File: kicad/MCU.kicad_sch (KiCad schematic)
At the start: 10 parts, among them U10 STM32G0B1KCUx, U34 SN65HVD230, Y2 CM9V-T1A 32.768 kHz

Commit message: Placed status LEDs
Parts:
- added D42: Status_LED1, symbol Device:LED
- added D43: Status_LED2, symbol Device:LED
- added R76, R77: 150, symbol Device:R
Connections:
- net GND: now also D42.1 (K), D43.1 (K)
- net NRST: now reaches U10.6 (PF2)
- net Status_LED1: no longer names the net of U10.30 (PB6)
- net Status_LED1: now also R76.2
- net Status_LED2: no longer names the net of U10.20 (PC6)
- net Status_LED2: now also R77.2
- new net: D43.2 (A), R77.1
- new net: D42.2 (A), R76.1
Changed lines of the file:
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@@
+    (stroke (width 0) (type default))
+  )
+  (wire (pts (xy 40.64 72.39) (xy 40.64 69.85))
     (stroke (width 0) (type default))
   )
@@
     (stroke (width 0) (type default))
   )
+  (wire (pts (xy 44.45 46.99) (xy 54.61 46.99))
+    (stroke (width 0) (type default))
+  )
   (wire (pts (xy 38.1 74.93) (xy 54.61 74.93))
     (stroke (width 0) (type default))
   )
+  (wire (pts (xy 54.61 72.39) (xy 40.64 72.39))
+    (stroke (width 0) (type default))
+  )
   (wire (pts (xy 151.13 78.74) (xy 151.13 76.2))
     (stroke (width 0) (type default))
   )
+  (wire (pts (xy 40.64 69.85) (xy 39.37 69.85))
+    (stroke (width 0) (type default))
+  )
   (wire (pts (xy 90.17 67.31) (xy 104.14 67.31))
     (stroke (width 0) (type default))
@@
     (stroke (width 0) (type default))
   )
-  (global_label "Status_LED2" (shape output) (at 54.61 46.99 180) (fields_autoplaced)
-    (effects (font (size 1.27 1.27)) (justify right))
-    (property "Intersheetrefs" "${INTERSHEET_REFS}" (at 40.0136 46.99 0)
-      (effects (font (size 1.27 1.27)) (justify right) hide)
-    )
-  )
   (global_label "ChargeEnable" (shape output) (at 54.61 59.69 180) (fields_autoplaced)
     (effects (font (size 1.27 1.27)) (justify right))
@@
     )
   )
+  (global_label "NRST" (shape input) (at 54.61 41.91 180) (fields_autoplaced)
+    (effects (font (size 1.27 1.27)) (justify right))
+    (property "Intersheetrefs" "${INTERSHEET_REFS}" (at 46.8472 41.91 0)
+      (effects (font (size 1.27 1.27)) (justify right) hide)
+    )
+  )
   (global_label "SWDCLK" (shape input) (at 90.17 77.47 0) (fields_autoplaced)
     (effects (font (size 1.27 1.27)) (justify left))
@@
     (effects (font (size 1.27 1.27)) (justify right))
     (property "Intersheetrefs" "${INTERSHEET_REFS}" (at 139.0129 76.2 0)
-      (effects (font (size 1.27 1.27)) (justify right) hide)
-    )
-  )
-  (global_label "Status_LED1" (shape output) (at 54.61 72.39 180) (fields_autoplaced)
-    (effects (font (size 1.27 1.27)) (justify right))
-    (property "Intersheetrefs" "${INTERSHEET_REFS}" (at 40.0136 72.39 0)
       (effects (font (size 1.27 1.27)) (justify right) hide)
     )
@@
         (path "/7f25f26f-13d1-483f-a85d-b3abae309e30/bb4c6abb-96c2-4de6-af9e-637895d0c9f4"
           (reference "C14") (unit 1)
+        )
+      )
+    )
+  )
+  (symbol (lib_id "Device:LED") (at 33.02 46.99 0) (unit 1)
+    (in_bom yes) (on_board yes) (dnp no) (fields_autoplaced)
+    (property "Reference" "D43" (at 31.4325 40.64 0)
+      (effects (font (size 1.27 1.27)))
+    )
+    (property "Value" "Status_LED2" (at 31.4325 43.18 0)
+      (effects (font (size 1.27 1.27)))
+    )
+    (property "Footprint" "" (at 33.02 46.99 0)
+      (effects (font (size 1.27 1.27)) hide)
+    )
+    (property "Datasheet" "~" (at 33.02 46.99 0)
+      (effects (font (size 1.27 1.27)) hide)
+    )
+    (pin "1")
+    (pin "2")
+    (instances
+      (project "sBMS"
+        (path "/7f25f26f-13d1-483f-a85d-b3abae309e30/bb4c6abb-96c2-4de6-af9e-637895d0c9f4"
+          (reference "D43") (unit 1)
         )
       )
@@
     )
   )
+  (symbol (lib_id "Device:R") (at 35.56 69.85 90) (unit 1)
+    (in_bom yes) (on_board yes) (dnp no) (fields_autoplaced)
+    (property "Reference" "R76" (at 35.56 63.5 90)
+      (effects (font (size 1.27 1.27)))
+    )
+    (property "Value" "150" (at 35.56 66.04 90)
+      (effects (font (size 1.27 1.27)))
+    )
+    (property "Footprint" "" (at 35.56 71.628 90)
+      (effects (font (size 1.27 1.27)) hide)
+    )
+    (property "Datasheet" "~" (at 35.56 69.85 0)
+      (effects (font (size 1.27 1.27)) hide)
+    )
+    (pin "1")
+    (pin "2")
+    (instances
+      (project "sBMS"
+        (path "/7f25f26f-13d1-483f-a85d-b3abae309e30/bb4c6abb-96c2-4de6-af9e-637895d0c9f4"
+          (reference "R76") (unit 1)
+        )
+      )
+    )
+  )
   (symbol (lib_id "power:GND") (at 138.43 46.99 270) (unit 1)
     (in_bom yes) (on_board yes) (dnp no) (fields_autoplaced)
@@
     )
   )
+  (symbol (lib_id "Device:LED") (at 27.94 69.85 0) (unit 1)
+    (in_bom yes) (on_board yes) (dnp no) (fields_autoplaced)
+    (property "Reference" "D42" (at 26.3525 63.5 0)
+      (effects (font (size 1.27 1.27)))
+    )
+    (property "Value" "Status_LED1" (at 26.3525 66.04 0)
+      (effects (font (size 1.27 1.27)))
+    )
+    (property "Footprint" "" (at 27.94 69.85 0)
+      (effects (font (size 1.27 1.27)) hide)
+    )
+    (property "Datasheet" "~" (at 27.94 69.85 0)
+      (effects (font (size 1.27 1.27)) hide)
+    )
+    (pin "1")
+    (pin "2")
+    (instances
+      (project "sBMS"
+        (path "/7f25f26f-13d1-483f-a85d-b3abae309e30/bb4c6abb-96c2-4de6-af9e-637895d0c9f4"
+          (reference "D42") (unit 1)
+        )
+      )
+    )
+  )
   (symbol (lib_id "power:+3.3V") (at 111.76 67.31 270) (unit 1)
     (in_bom yes) (on_board yes) (dnp no) (fields_autoplaced)
@@
         )
       )
+    )
+  )
+  (symbol (lib_id "power:GND") (at 29.21 46.99 270) (unit 1)
+    (in_bom yes) (on_board yes) (dnp no) (fields_autoplaced)
+    (property "Reference" "#PWR0154" (at 22.86 46.99 0)
+      (effects (font (size 1.27 1.27)) hide)
+    )
+    (property "Value" "GND" (at 25.4 46.99 90)
+      (effects (font (size 1.27 1.27)) (justify right))
+    )
+    (property "Footprint" "" (at 29.21 46.99 0)
+      (effects (font (size 1.27 1.27)) hide)
+    )
+    (property "Datasheet" "" (at 29.21 46.99 0)
+      (effects (font (size 1.27 1.27)) hide)
+    )
+    (pin "1")
+    (instances
+      (project "sBMS"
+        (path "/7f25f26f-13d1-483f-a85d-b3abae309e30/bb4c6abb-96c2-4de6-af9e-637895d0c9f4"
+          (reference "#PWR0154") (unit 1)
+        )
+      )
+    )
+  )
+  (symbol (lib_id "power:GND") (at 24.13 69.85 270) (unit 1)
+    (in_bom yes) (on_board yes) (dnp no) (fields_autoplaced)
+    (property "Reference" "#PWR0153" (at 17.78 69.85 0)
+      (effects (font (size 1.27 1.27)) hide)
+    )
+    (property "Value" "GND" (at 20.32 69.85 90)
+      (effects (font (size 1.27 1.27)) (justify right))
+    )
+    (property "Footprint" "" (at 24.13 69.85 0)
+      (effects (font (size 1.27 1.27)) hide)
+    )
+    (property "Datasheet" "" (at 24.13 69.85 0)
+      (effects (font (size 1.27 1.27)) hide)
+    )
+    (pin "1")
+    (instances
+      (project "sBMS"
+        (path "/7f25f26f-13d1-483f-a85d-b3abae309e30/bb4c6abb-96c2-4de6-af9e-637895d0c9f4"
+          (reference "#PWR0153") (unit 1)
+        )
+      )
+    )
+  )
+  (symbol (lib_id "Device:R") (at 40.64 46.99 90) (unit 1)
+    (in_bom yes) (on_board yes) (dnp no) (fields_autoplaced)
+    (property "Reference" "R77" (at 40.64 40.64 90)
+      (effects (font (size 1.27 1.27)))
+    )
+    (property "Value" "150" (at 40.64 43.18 90)
+      (effects (font (size 1.27 1.27)))
+    )
+    (property "Footprint" "" (at 40.64 48.768 90)
+      (effects (font (size 1.27 1.27)) hide)
+    )
+    (property "Datasheet" "~" (at 40.64 46.99 0)
+      (effects (font (size 1.27 1.27)) hide)
+    )
+    (pin "1")
+    (pin "2")
+    (instances
+      (project "sBMS"
+        (path "/7f25f26f-13d1-483f-a85d-b3abae309e30/bb4c6abb-96c2-4de6-af9e-637895d0c9f4"
+          (reference "R77") (unit 1)
+        )
+      )

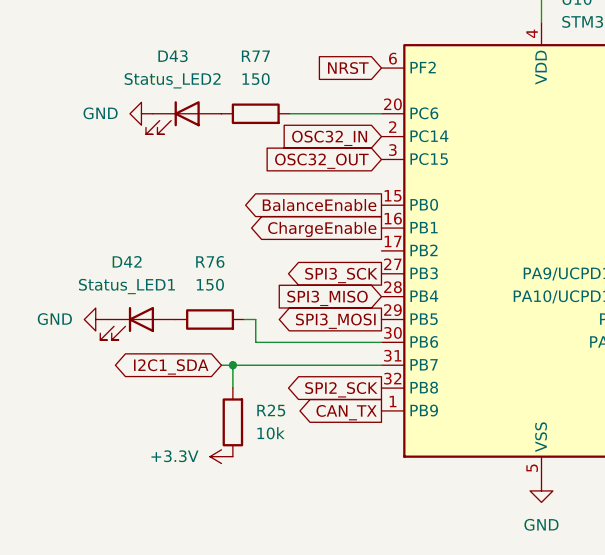
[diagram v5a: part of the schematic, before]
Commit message: Added charge MOSFET
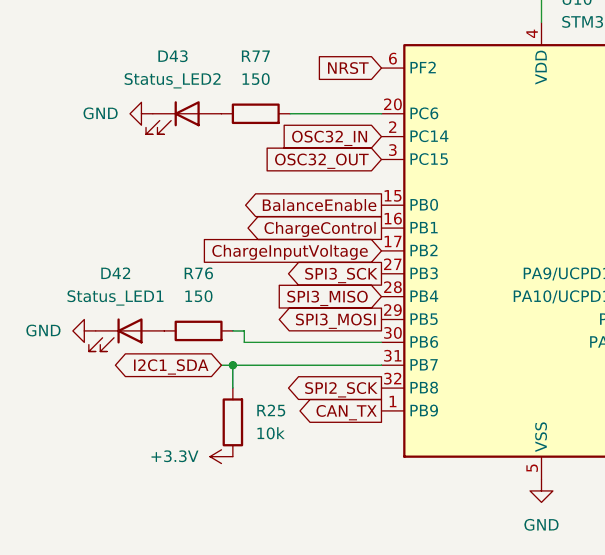
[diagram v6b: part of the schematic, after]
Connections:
- net ChargeInputVoltage: now reaches U10.17 (PB2)
- net ChargeEnable renamed ChargeControl
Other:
- moved on the sheet: D42, R76
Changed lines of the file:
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@@
   (title_block
     (title "Logic")
-    (date "2023-08-20")
+    (date "2023-09-06")
     (rev "1")
     (company "Dynamium")
@@
     (stroke (width 0) (type default))
   )
-  (wire (pts (xy 40.64 72.39) (xy 40.64 69.85))
+  (wire (pts (xy 39.37 72.39) (xy 54.61 72.39))
     (stroke (width 0) (type default))
   )
@@
     (stroke (width 0) (type default))
   )
-  (wire (pts (xy 54.61 72.39) (xy 40.64 72.39))
+  (wire (pts (xy 38.1 71.12) (xy 39.37 71.12))
     (stroke (width 0) (type default))
   )
@@
     (stroke (width 0) (type default))
   )
-  (wire (pts (xy 40.64 69.85) (xy 39.37 69.85))
+  (wire (pts (xy 39.37 71.12) (xy 39.37 72.39))
     (stroke (width 0) (type default))
   )
@@
     (stroke (width 0) (type default))
   )
-  (global_label "ChargeEnable" (shape output) (at 54.61 59.69 180) (fields_autoplaced)
-    (effects (font (size 1.27 1.27)) (justify right))
-    (property "Intersheetrefs" "${INTERSHEET_REFS}" (at 38.6832 59.69 0)
+  (global_label "ChargeControl" (shape output) (at 54.61 59.69 180) (fields_autoplaced)
+    (effects (font (size 1.27 1.27)) (justify right))
+    (property "Intersheetrefs" "${INTERSHEET_REFS}" (at 38.1389 59.69 0)
       (effects (font (size 1.27 1.27)) (justify right) hide)
     )
@@
     (property "Intersheetrefs" "${INTERSHEET_REFS}" (at 175.3424 44.45 0)
       (effects (font (size 1.27 1.27)) (justify left) hide)
+    )
+  )
+  (global_label "ChargeInputVoltage" (shape input) (at 54.61 62.23 180) (fields_autoplaced)
+    (effects (font (size 1.27 1.27)) (justify right))
+    (property "Intersheetrefs" "${INTERSHEET_REFS}" (at 33.2404 62.23 0)
+      (effects (font (size 1.27 1.27)) (justify right) hide)
     )
   )
@@
     )
   )
-  (symbol (lib_id "Device:R") (at 35.56 69.85 90) (unit 1)
-    (in_bom yes) (on_board yes) (dnp no) (fields_autoplaced)
-    (property "Reference" "R76" (at 35.56 63.5 90)
-      (effects (font (size 1.27 1.27)))
-    )
-    (property "Value" "150" (at 35.56 66.04 90)
-      (effects (font (size 1.27 1.27)))
-    )
-    (property "Footprint" "" (at 35.56 71.628 90)
-      (effects (font (size 1.27 1.27)) hide)
-    )
-    (property "Datasheet" "~" (at 35.56 69.85 0)
+  (symbol (lib_id "Device:R") (at 34.29 71.12 90) (unit 1)
+    (in_bom yes) (on_board yes) (dnp no) (fields_autoplaced)
+    (property "Reference" "R76" (at 34.29 64.77 90)
+      (effects (font (size 1.27 1.27)))
+    )
+    (property "Value" "150" (at 34.29 67.31 90)
+      (effects (font (size 1.27 1.27)))
+    )
+    (property "Footprint" "" (at 34.29 72.898 90)
+      (effects (font (size 1.27 1.27)) hide)
+    )
+    (property "Datasheet" "~" (at 34.29 71.12 0)
       (effects (font (size 1.27 1.27)) hide)
     )
@@
     )
   )
-  (symbol (lib_id "Device:LED") (at 27.94 69.85 0) (unit 1)
-    (in_bom yes) (on_board yes) (dnp no) (fields_autoplaced)
-    (property "Reference" "D42" (at 26.3525 63.5 0)
-      (effects (font (size 1.27 1.27)))
-    )
-    (property "Value" "Status_LED1" (at 26.3525 66.04 0)
-      (effects (font (size 1.27 1.27)))
-    )
-    (property "Footprint" "" (at 27.94 69.85 0)
-      (effects (font (size 1.27 1.27)) hide)
-    )
-    (property "Datasheet" "~" (at 27.94 69.85 0)
+  (symbol (lib_id "Device:LED") (at 26.67 71.12 0) (unit 1)
+    (in_bom yes) (on_board yes) (dnp no) (fields_autoplaced)
+    (property "Reference" "D42" (at 25.0825 64.77 0)
+      (effects (font (size 1.27 1.27)))
+    )
+    (property "Value" "Status_LED1" (at 25.0825 67.31 0)
+      (effects (font (size 1.27 1.27)))
+    )
+    (property "Footprint" "" (at 26.67 71.12 0)
+      (effects (font (size 1.27 1.27)) hide)
+    )
+    (property "Datasheet" "~" (at 26.67 71.12 0)
       (effects (font (size 1.27 1.27)) hide)
     )
@@
     )
   )
-  (symbol (lib_id "power:GND") (at 24.13 69.85 270) (unit 1)
-    (in_bom yes) (on_board yes) (dnp no) (fields_autoplaced)
-    (property "Reference" "#PWR0153" (at 17.78 69.85 0)
-      (effects (font (size 1.27 1.27)) hide)
-    )
-    (property "Value" "GND" (at 20.32 69.85 90)
+  (symbol (lib_id "power:GND") (at 22.86 71.12 270) (unit 1)
+    (in_bom yes) (on_board yes) (dnp no) (fields_autoplaced)
+    (property "Reference" "#PWR0153" (at 16.51 71.12 0)
+      (effects (font (size 1.27 1.27)) hide)
+    )
+    (property "Value" "GND" (at 19.05 71.12 90)
       (effects (font (size 1.27 1.27)) (justify right))
     )
-    (property "Footprint" "" (at 24.13 69.85 0)
-      (effects (font (size 1.27 1.27)) hide)
-    )
-    (property "Datasheet" "" (at 24.13 69.85 0)
-      (effects (font (size 1.27 1.27)) hide)
-    )
+    (property "Footprint" "" (at 22.86 71.12 0)
+      (effects (font (size 1.27 1.27)) hide)
+    )
+    (property "Datasheet" "" (at 22.86 71.12 0)
+      (effects (font (size 1.27 1.27)) hide)
+    )
